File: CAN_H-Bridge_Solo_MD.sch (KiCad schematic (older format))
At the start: 48 parts, among them IC1 SI8650AB-B-IS1, IC2 A3921KLPTR-T, IC3 AP7381-50SA-7, J2 Conn_01x03, J3 Conn_01x05, J4 Bus_mechaken_PCIexpress_x16_1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, M1 Motor_DC, Q1 IRFB3806PBF, Q2 IRFB3806PBF, Q3 IRFB3806PBF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

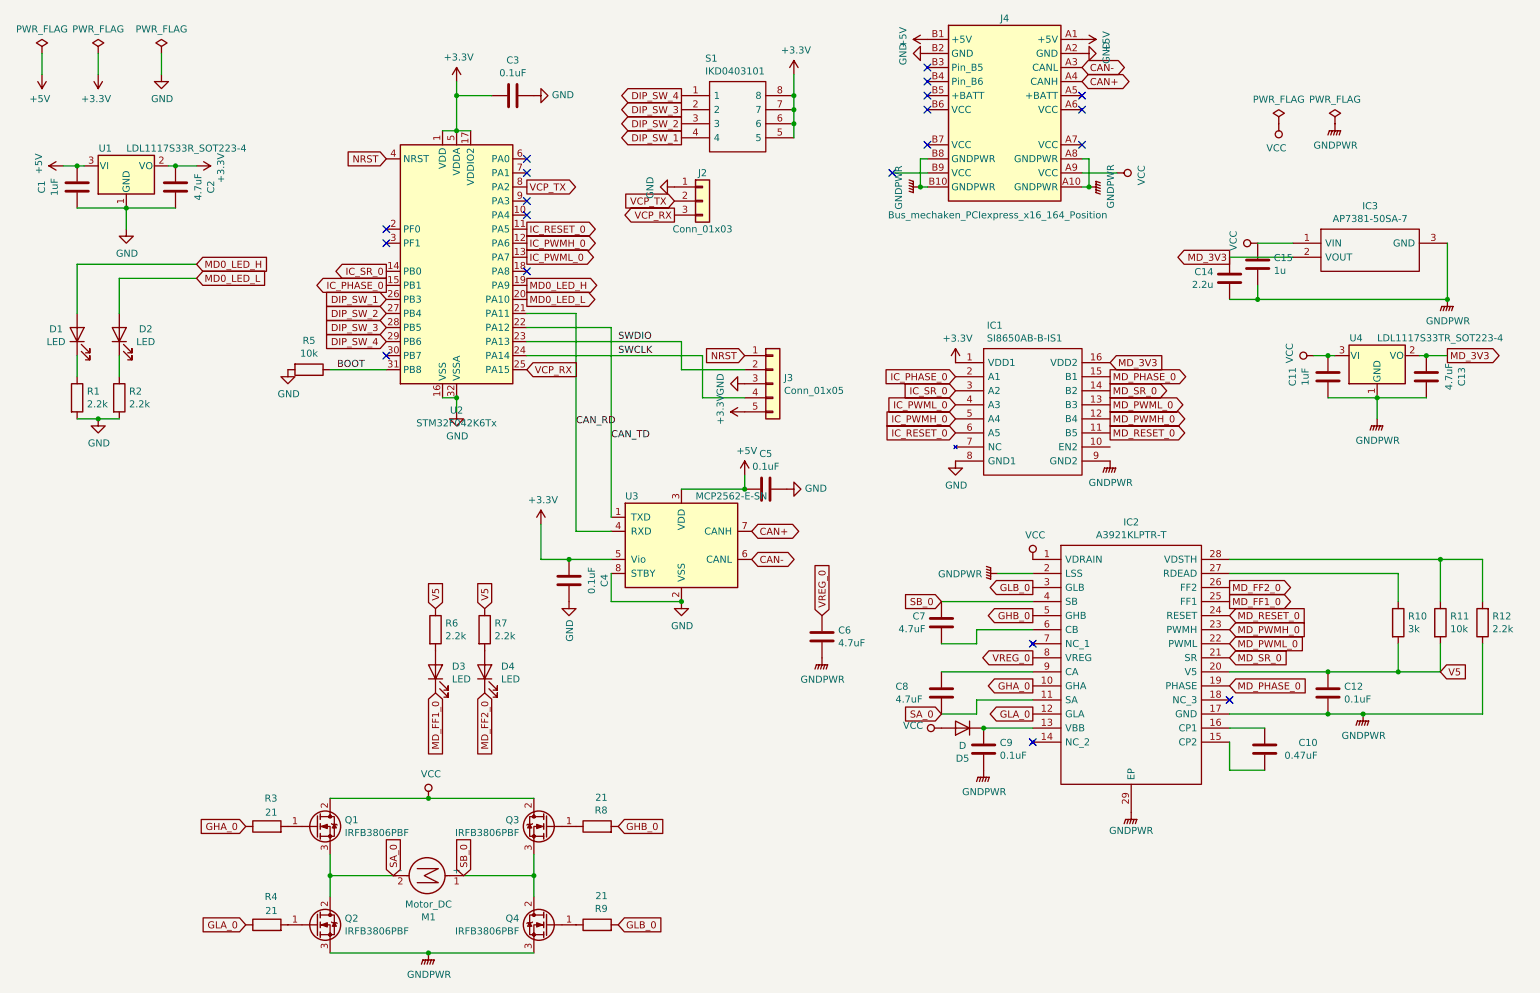
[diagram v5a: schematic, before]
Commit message: add
LDOの逆電圧防止用にSBDを追加
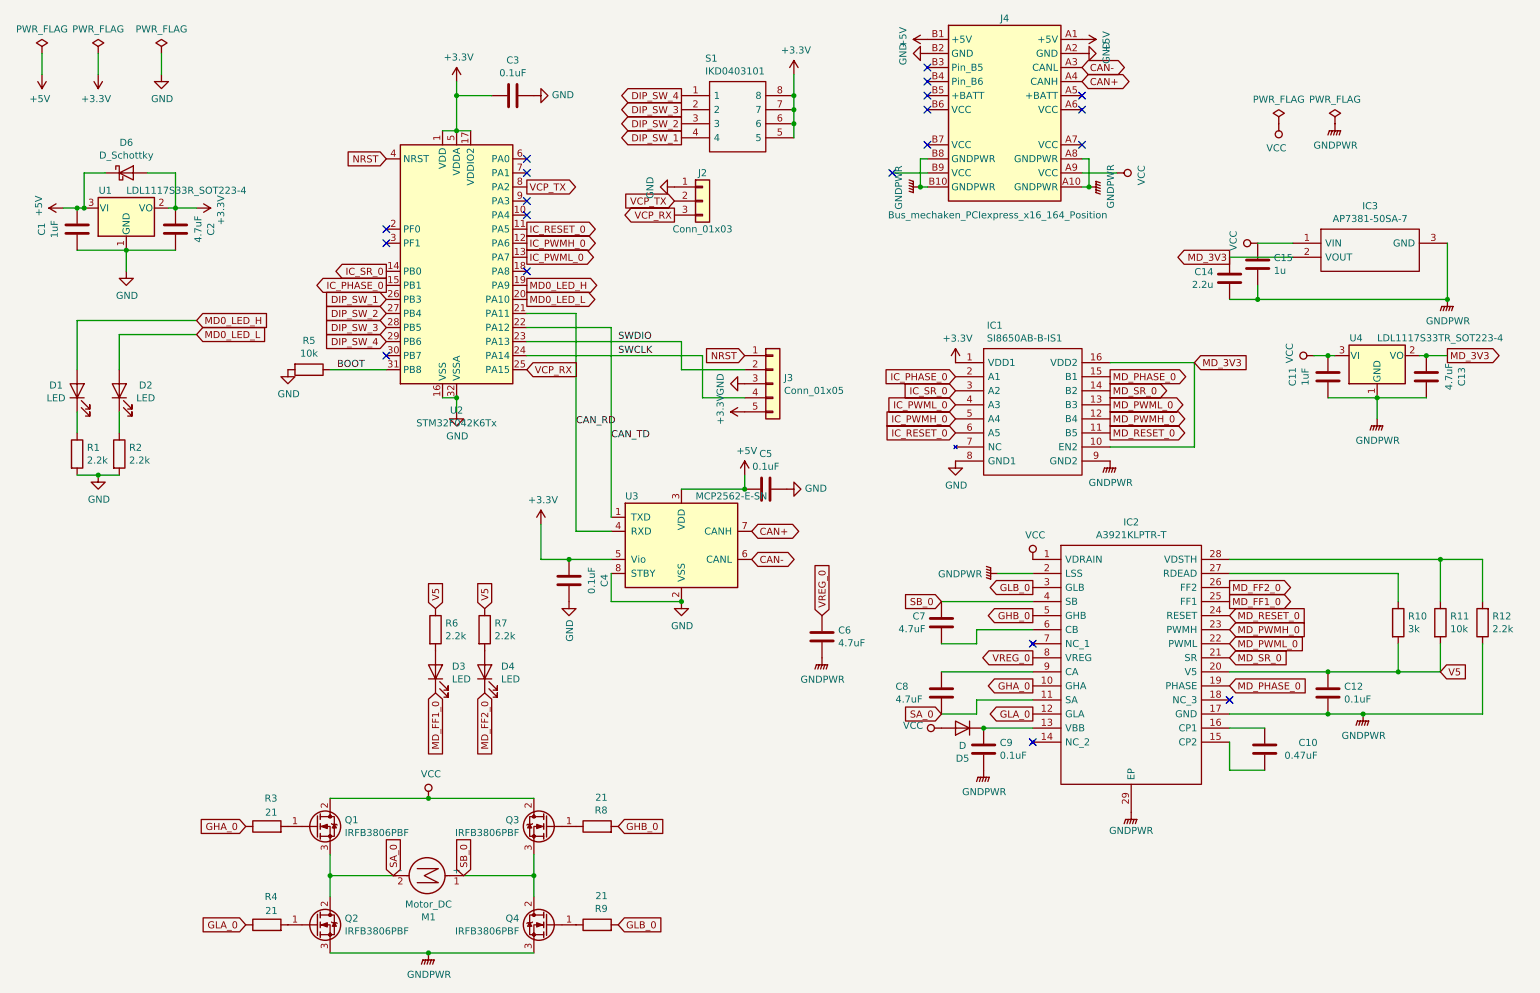
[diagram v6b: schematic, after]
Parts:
- added D6: D_Schottky, Diode_SMD:D_0603_1608Metric_Pad1.05x0.95mm_HandSolder, symbol Device:D_Schottky
- D5: footprint LED_SMD:LED_0603_1608Metric_Castellated -> Diode_SMD:D_0603_1608Metric_Pad1.05x0.95mm_HandSolder
- IC3: footprint SOT96P240X105-3N -> SamacSys_Parts:SOT96P240X105-3N
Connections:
- net +3V3: now also D6.2 (A)
- net +5V: now also D6.1 (K)
- net MD_3V3: now also IC1.10 (EN2)
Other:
- moved on the sheet: C1, C2, D1, D2, R1, R2, U1
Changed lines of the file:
@@
 F 0 "D5" H 7300 5866 50  0000 C CNN
 F 1 "D" H 7300 5775 50  0000 C CNN
-F 2 "LED_SMD:LED_0603_1608Metric_Castellated" H 7300 5650 50  0001 C CNN
+F 2 "Diode_SMD:D_0603_1608Metric_Pad1.05x0.95mm_HandSolder" H 7300 5650 50  0001 C CNN
 F 3 "~" H 7300 5650 50  0001 C CNN
 	1    7300 5650
@@
 	1600 1000 1600 850
 Wire Wire Line
-	1000 1650 1050 1650
-Connection ~ 1000 1650
-Wire Wire Line
-	1700 1650 1850 1650
-Connection ~ 1700 1650
-Wire Wire Line
-	1700 1950 1350 1950
-Wire Wire Line
-	1350 1950 1000 1950
-Connection ~ 1350 1950
-Wire Wire Line
-	1350 1950 1350 2100
-Wire Wire Line
-	1650 1650 1700 1650
-Wire Wire Line
-	900  1650 1000 1650
+	1000 1950 1050 1950
+Connection ~ 1000 1950
+Wire Wire Line
+	1700 1950 1850 1950
+Connection ~ 1700 1950
+Wire Wire Line
+	1700 2250 1350 2250
+Wire Wire Line
+	1350 2250 1000 2250
+Connection ~ 1350 2250
+Wire Wire Line
+	1350 2250 1350 2400
+Wire Wire Line
+	1650 1950 1700 1950
+Wire Wire Line
+	900  1950 1000 1950
 Wire Wire Line
 	3700 1150 3950 1150
@@
 L Device:C C1
 U 1 1 5DA7A5B9
-P 1000 1800
-F 0 "C1" V 748 1800 50  0000 C CNN
-F 1 "1uF" V 839 1800 50  0000 C CNN
-F 2 "Capacitor_SMD:C_0805_2012Metric_Pad1.15x1.40mm_HandSolder" H 1038 1650 50  0001 C CNN
-F 3 "~" H 1000 1800 50  0001 C CNN
-	1    1000 1800
+P 1000 2100
+F 0 "C1" V 748 2100 50  0000 C CNN
+F 1 "1uF" V 839 2100 50  0000 C CNN
+F 2 "Capacitor_SMD:C_0805_2012Metric_Pad1.15x1.40mm_HandSolder" H 1038 1950 50  0001 C CNN
+F 3 "~" H 1000 2100 50  0001 C CNN
+	1    1000 2100
 	1    0    0    -1
 $EndComp
@@
 L Device:C C2
 U 1 1 5DA788D5
-P 1700 1800
-F 0 "C2" V 1448 1800 50  0000 C CNN
-F 1 "4.7uF" V 1539 1800 50  0000 C CNN
-F 2 "Capacitor_SMD:C_0805_2012Metric_Pad1.15x1.40mm_HandSolder" H 1738 1650 50  0001 C CNN
-F 3 "~" H 1700 1800 50  0001 C CNN
-	1    1700 1800
+P 1700 2100
+F 0 "C2" V 1448 2100 50  0000 C CNN
+F 1 "4.7uF" V 1539 2100 50  0000 C CNN
+F 2 "Capacitor_SMD:C_0805_2012Metric_Pad1.15x1.40mm_HandSolder" H 1738 1950 50  0001 C CNN
+F 3 "~" H 1700 2100 50  0001 C CNN
+	1    1700 2100
 	-1   0    0    1
 $EndComp
@@
 VCP_RX
 $Comp
-L Device:LED D1
-U 1 1 5D5ECBC3
-P 1000 2850
-F 0 "D1" V 1039 3000 50  0000 C CNN
-F 1 "LED" V 948 3000 50  0000 C CNN
-F 2 "LED_SMD:LED_0603_1608Metric_Castellated" H 1000 2850 50  0001 C CNN
-F 3 "~" H 1000 2850 50  0001 C CNN
-	1    1000 2850
-	0    -1   -1   0
-$EndComp
-$Comp
 L power:GND #PWR05
 U 1 1 5D63F689
-P 1350 2100
-F 0 "#PWR05" H 1350 1850 50  0001 C CNN
-F 1 "GND" H 1355 1927 50  0000 C CNN
-F 2 "" H 1350 2100 50  0001 C CNN
-F 3 "" H 1350 2100 50  0001 C CNN
-	1    1350 2100
+P 1350 2400
+F 0 "#PWR05" H 1350 2150 50  0001 C CNN
+F 1 "GND" H 1355 2227 50  0000 C CNN
+F 2 "" H 1350 2400 50  0001 C CNN
+F 3 "" H 1350 2400 50  0001 C CNN
+	1    1350 2400
 	1    0    0    -1
 $EndComp
@@
 L power:+3.3V #PWR07
 U 1 1 5D635307
-P 1850 1650
-F 0 "#PWR07" H 1850 1500 50  0001 C CNN
-F 1 "+3.3V" H 1865 1823 50  0000 C CNN
-F 2 "" H 1850 1650 50  0001 C CNN
-F 3 "" H 1850 1650 50  0001 C CNN
-	1    1850 1650
+P 1850 1950
+F 0 "#PWR07" H 1850 1800 50  0001 C CNN
+F 1 "+3.3V" H 1865 2123 50  0000 C CNN
+F 2 "" H 1850 1950 50  0001 C CNN
+F 3 "" H 1850 1950 50  0001 C CNN
+	1    1850 1950
 	0    1    1    0
 $EndComp
@@
 L power:+5V #PWR02
 U 1 1 5D62D67A
-P 900 1650
-F 0 "#PWR02" H 900 1500 50  0001 C CNN
-F 1 "+5V" H 915 1823 50  0000 C CNN
-F 2 "" H 900 1650 50  0001 C CNN
-F 3 "" H 900 1650 50  0001 C CNN
-	1    900  1650
+P 900 1950
+F 0 "#PWR02" H 900 1800 50  0001 C CNN
+F 1 "+5V" H 915 2123 50  0000 C CNN
+F 2 "" H 900 1950 50  0001 C CNN
+F 3 "" H 900 1950 50  0001 C CNN
+	1    900  1950
 	0    -1   -1   0
 $EndComp
@@
 $EndComp
 $Comp
-L power:GND #PWR04
-U 1 1 5D5E9892
-P 1150 3450
-F 0 "#PWR04" H 1150 3200 50  0001 C CNN
-F 1 "GND" H 1155 3277 50  0000 C CNN
-F 2 "" H 1150 3450 50  0001 C CNN
-F 3 "" H 1150 3450 50  0001 C CNN
-	1    1150 3450
-	1    0    0    -1
-$EndComp
-$Comp
 L Device:R R5
 U 1 1 5D5AB267
@@
 	1    2650 3100
 	0    1    1    0
-$EndComp
-$Comp
-L power:GND #PWR08
-U 1 1 5D5AAC2B
-P 2500 3100
-F 0 "#PWR08" H 2500 2850 50  0001 C CNN
-F 1 "GND" H 2505 2927 50  0000 C CNN
-F 2 "" H 2500 3100 50  0001 C CNN
-F 3 "" H 2500 3100 50  0001 C CNN
-	1    2500 3100
-	1    0    0    -1
 $EndComp
 $Comp
@@
 DIP_SW_1
 Wire Wire Line
-	1850 2450 1300 2450
-Wire Wire Line
-	1300 2450 1300 2700
-Wire Wire Line
-	1000 2700 1000 2350
-Wire Wire Line
 	5750 3100 5300 3100
 Wire Wire Line
@@
 L H-Bridge-MD-rescue:LD1117S33TR_SOT223-Regulator_Linear U1
 U 1 1 5DEBD597
-P 1350 1650
-F 0 "U1" H 1200 1775 50  0000 C CNN
-F 1 "LDL1117S33R_SOT223-4" H 1350 1775 50  0000 L CNN
-F 2 "Package_TO_SOT_SMD:SOT-223-3_TabPin2" H 1350 1850 50  0001 C CNN
-F 3 "http://www.st.com/st-web-ui/static/active/en/resource/technical/document/datasheet/CD00000544.pdf" H 1450 1400 50  0001 C CNN
-	1    1350 1650
-	1    0    0    -1
-$EndComp
-Wire Wire Line
-	1000 2350 1850 2350
-Wire Wire Line
-	1000 3000 1000 3150
-Wire Wire Line
-	1300 3150 1300 3000
+P 1350 1950
+F 0 "U1" H 1200 2075 50  0000 C CNN
+F 1 "LDL1117S33R_SOT223-4" H 1350 2075 50  0000 L CNN
+F 2 "Package_TO_SOT_SMD:SOT-223-3_TabPin2" H 1350 2150 50  0001 C CNN
+F 3 "http://www.st.com/st-web-ui/static/active/en/resource/technical/document/datasheet/CD00000544.pdf" H 1450 1700 50  0001 C CNN
+	1    1350 1950
+	1    0    0    -1
+$EndComp
 $Comp
 L power:+5V #PWR027
@@
 	1    0    0    -1
 $EndComp
-Text GLabel 8350 3050 2    50   Input ~ 0
+Text GLabel 8950 3050 2    50   Input ~ 0
 MD_3V3
 Text GLabel 3900 5400 3    50   Input ~ 0
@@
 $EndComp
 $Comp
-L Device:R R2
-U 1 1 5E0C5428
-P 1300 3300
-F 0 "R2" H 1370 3346 50  0000 L CNN
-F 1 "2.2k" H 1370 3255 50  0000 L CNN
-F 2 "Resistor_SMD:R_0603_1608Metric_Pad1.05x0.95mm_HandSolder" V 1230 3300 50  0001 C CNN
-F 3 "~" H 1300 3300 50  0001 C CNN
-	1    1300 3300
-	1    0    0    -1
-$EndComp
-$Comp
-L Device:R R1
-U 1 1 5E0C542E
-P 1000 3300
-F 0 "R1" H 1070 3346 50  0000 L CNN
-F 1 "2.2k" H 1070 3255 50  0000 L CNN
-F 2 "Resistor_SMD:R_0603_1608Metric_Pad1.05x0.95mm_HandSolder" V 930 3300 50  0001 C CNN
-F 3 "~" H 1000 3300 50  0001 C CNN
-	1    1000 3300
-	1    0    0    -1
-$EndComp
-Wire Wire Line
-	1300 3450 1150 3450
-$Comp
-L Device:LED D2
-U 1 1 5D5EBAF7
-P 1300 2850
-F 0 "D2" V 1339 2662 50  0000 C CNN
-F 1 "LED" V 1248 2662 50  0000 C CNN
-F 2 "LED_SMD:LED_0603_1608Metric_Castellated" H 1300 2850 50  0001 C CNN
-F 3 "~" H 1300 2850 50  0001 C CNN
-	1    1300 2850
-	0    -1   -1   0
-$EndComp
-Connection ~ 1150 3450
-Wire Wire Line
-	1150 3450 1000 3450
-$Comp
 L Transistor_FET:IRLB8721PBF Q2
 U 1 1 5E0F4419
@@
 F 0 "IC3" H 10200 2465 50  0000 C CNN
 F 1 "AP7381-50SA-7" H 10200 2374 50  0000 C CNN
-F 2 "SOT96P240X105-3N" H 10600 2300 50  0001 L CNN
+F 2 "SamacSys_Parts:SOT96P240X105-3N" H 10600 2300 50  0001 L CNN
 F 3 "https://componentsearchengine.com/Datasheets/1/AP7381-50SA-7.pdf" H 10600 2200 50  0001 L CNN
 F 4 "LDO Voltage Regulators LDO CMOS LowCurr SOT23 T&R 3K" H 10600 2100 50  0001 L CNN "Description"
@@
 Text GLabel 9200 2300 0    50   Output ~ 0
 MD_3V3
-Text GLabel 1850 2350 2    50   Input ~ 0
+Wire Wire Line
+	8350 3050 8950 3050
+Wire Wire Line
+	8350 3650 8950 3650
+Wire Wire Line
+	8950 3650 8950 3050
+$Comp
+L Device:D_Schottky D6
+U 1 1 5E5159FF
+P 1350 1700
+F 0 "D6" H 1350 1916 50  0000 C CNN
+F 1 "D_Schottky" H 1350 1825 50  0000 C CNN
+F 2 "Diode_SMD:D_0603_1608Metric_Pad1.05x0.95mm_HandSolder" H 1350 1700 50  0001 C CNN
+F 3 "~" H 1350 1700 50  0001 C CNN
+	1    1350 1700
+	1    0    0    -1
+$EndComp
+Text GLabel 1850 2850 2    50   Input ~ 0
+MD0_LED_L
+Text GLabel 1850 2750 2    50   Input ~ 0
 MD0_LED_H
-Text GLabel 1850 2450 2    50   Input ~ 0
-MD0_LED_L
+Wire Wire Line
+	1150 3850 1000 3850
+Connection ~ 1150 3850
+$Comp
+L Device:LED D2
+U 1 1 5D5EBAF7
+P 1300 3250
+F 0 "D2" V 1339 3062 50  0000 C CNN
+F 1 "LED" V 1248 3062 50  0000 C CNN
+F 2 "LED_SMD:LED_0603_1608Metric_Castellated" H 1300 3250 50  0001 C CNN
+F 3 "~" H 1300 3250 50  0001 C CNN
+	1    1300 3250
+	0    -1   -1   0
+$EndComp
+Wire Wire Line
+	1300 3850 1150 3850
+$Comp
+L Device:R R1
+U 1 1 5E0C542E
+P 1000 3700
+F 0 "R1" H 1070 3746 50  0000 L CNN
+F 1 "2.2k" H 1070 3655 50  0000 L CNN
+F 2 "Resistor_SMD:R_0603_1608Metric_Pad1.05x0.95mm_HandSolder" V 930 3700 50  0001 C CNN
+F 3 "~" H 1000 3700 50  0001 C CNN
+	1    1000 3700
+	1    0    0    -1
+$EndComp
+$Comp
+L Device:R R2
+U 1 1 5E0C5428
+P 1300 3700
+F 0 "R2" H 1370 3746 50  0000 L CNN
+F 1 "2.2k" H 1370 3655 50  0000 L CNN
+F 2 "Resistor_SMD:R_0603_1608Metric_Pad1.05x0.95mm_HandSolder" V 1230 3700 50  0001 C CNN
+F 3 "~" H 1300 3700 50  0001 C CNN
+	1    1300 3700
+	1    0    0    -1
+$EndComp
+Wire Wire Line
+	1300 3550 1300 3400
+Wire Wire Line
+	1000 3400 1000 3550
+Wire Wire Line
+	1000 2750 1850 2750
+Wire Wire Line
+	1000 3100 1000 2750
+Wire Wire Line
+	1300 2850 1300 3100
+Wire Wire Line
+	1850 2850 1300 2850
+$Comp
+L power:GND #PWR08
+U 1 1 5D5AAC2B
+P 2500 3100
+F 0 "#PWR08" H 2500 2850 50  0001 C CNN
+F 1 "GND" H 2505 2927 50  0000 C CNN
+F 2 "" H 2500 3100 50  0001 C CNN
+F 3 "" H 2500 3100 50  0001 C CNN
+	1    2500 3100
+	1    0    0    -1
+$EndComp
+$Comp
+L power:GND #PWR04
+U 1 1 5D5E9892
+P 1150 3850
+F 0 "#PWR04" H 1150 3600 50  0001 C CNN
+F 1 "GND" H 1155 3677 50  0000 C CNN
+F 2 "" H 1150 3850 50  0001 C CNN
+F 3 "" H 1150 3850 50  0001 C CNN
+	1    1150 3850
+	1    0    0    -1
+$EndComp
+$Comp
+L Device:LED D1
+U 1 1 5D5ECBC3
+P 1000 3250
+F 0 "D1" V 1039 3400 50  0000 C CNN
+F 1 "LED" V 948 3400 50  0000 C CNN
+F 2 "LED_SMD:LED_0603_1608Metric_Castellated" H 1000 3250 50  0001 C CNN
+F 3 "~" H 1000 3250 50  0001 C CNN
+	1    1000 3250
+	0    -1   -1   0
+$EndComp
+Wire Wire Line
+	1050 1950 1050 1700
+Wire Wire Line
+	1050 1700 1200 1700
+Connection ~ 1050 1950
+Wire Wire Line
+	1500 1700 1700 1700
+Wire Wire Line
+	1700 1700 1700 1950
 $EndSCHEMATC

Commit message: clean
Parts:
- J3: value Conn_01x05 -> Conthrough
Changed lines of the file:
@@
 P 5950 3200
 F 0 "J3" H 6030 3242 50  0000 L CNN
-F 1 "Conn_01x05" H 6030 3151 50  0000 L CNN
+F 1 "Conthrough" H 6030 3151 50  0000 L CNN
 F 2 "Connector_PinHeader_2.54mm:PinHeader_1x05_P2.54mm_Vertical" H 5950 3200 50  0001 C CNN
 F 3 "~" H 5950 3200 50  0001 C CNN

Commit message: fix
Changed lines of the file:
@@
 Wire Wire Line
 	2800 6700 2800 6850
-Text GLabel 3750 6700 1    50   Input ~ 0
+Text GLabel 4250 6700 2    50   Output ~ 0
 SB_0
-Text GLabel 3250 6700 1    50   Input ~ 0
-SA_0
 Wire Wire Line
 	7050 1600 7000 1600
@@
 NoConn ~ 3200 3000
 NoConn ~ 6800 1700
-$Comp
-L Motor:Motor_DC M1
-U 1 1 5E054D53
-P 3550 6700
-F 0 "M1" V 3845 6650 50  0000 C CNN
-F 1 "Motor_DC" V 3754 6650 50  0000 C CNN
-F 2 "XT60:XT60PW" H 3550 6610 50  0001 C CNN
-F 3 "~" H 3550 6610 50  0001 C CNN
-	1    3550 6700
-	0    1    1    0
-$EndComp
 Wire Wire Line
 	3750 6700 4250 6700
-Wire Wire Line
-	2800 6700 3250 6700
 Text GLabel 10700 5250 2    50   Input ~ 0
 V5
@@
 Wire Wire Line
 	1700 1700 1700 1950
+Wire Wire Line
+	2800 6700 3250 6700
+$Comp
+L Motor:Motor_DC M1
+U 1 1 5E054D53
+P 3550 6700
+F 0 "M1" V 3845 6650 50  0000 C CNN
+F 1 "Motor_DC" V 3754 6650 50  0000 C CNN
+F 2 "XT60:XT60PW" H 3550 6610 50  0001 C CNN
+F 3 "~" H 3550 6610 50  0001 C CNN
+	1    3550 6700
+	0    1    1    0
+$EndComp
+Text GLabel 2800 6700 0    50   Output ~ 0
+SA_0
 $EndSCHEMATC
